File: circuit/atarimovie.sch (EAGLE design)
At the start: 11 parts, among them X1 22-23-2051

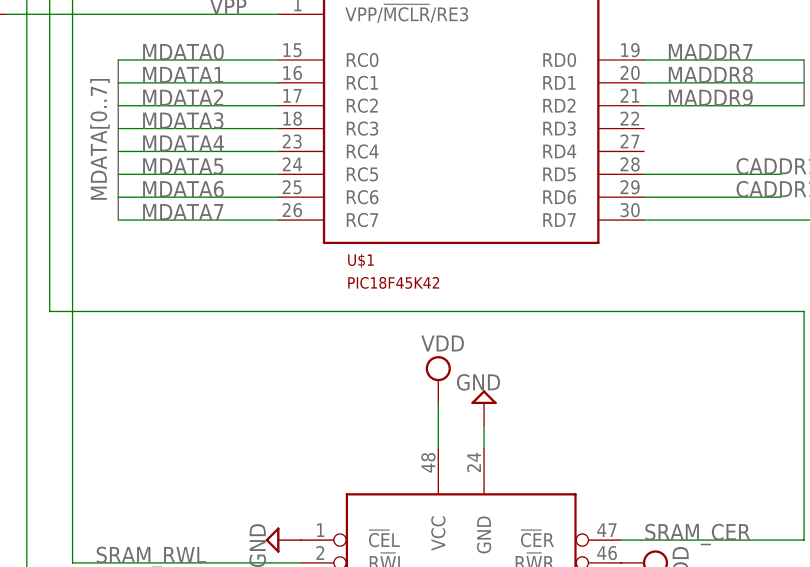
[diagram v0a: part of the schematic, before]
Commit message: Using PIC18F47K42 not PIC18F45K42
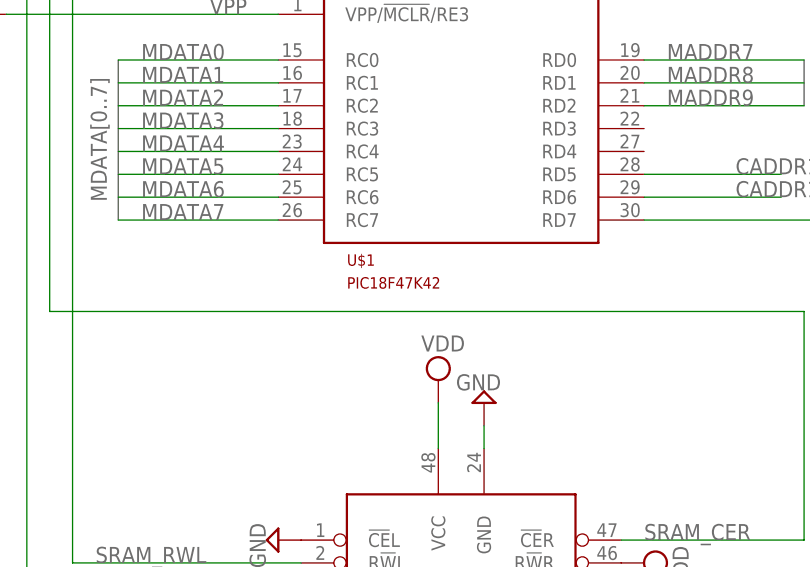
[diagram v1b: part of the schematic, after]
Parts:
- U$1: value PIC18F45K42 -> PIC18F47K42; device atari:PIC18F45K42 -> atari:PIC18F47K42
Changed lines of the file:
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@@
 </classes>
 <parts>
-<part name="U$1" library="atari" deviceset="PIC18F45K42" device=""/>
+<part name="U$1" library="atari" deviceset="PIC18F47K42" device=""/>
 <part name="U$2" library="atari" deviceset="7130LA35PDG" device=""/>
 <part name="SUPPLY1" library="supply2" library_urn="urn:adsk.eagle:library:372" deviceset="VDD" device=""/>
